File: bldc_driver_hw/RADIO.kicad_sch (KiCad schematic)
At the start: 0 parts

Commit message: wip
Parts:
- added C17: 10uF, Capacitor_SMD:C_0805_2012Metric_Pad1.18x1.45mm_HandSolder, symbol Device:C_Small
- added C18: 100nF, Capacitor_SMD:C_0603_1608Metric_Pad1.08x0.95mm_HandSolder, symbol Device:C_Small
- added D2, D3: LED, LED_SMD:LED_0603_1608Metric, symbol Device:LED
- added R10, R11, R12, R13, R14, R7, R8, R9: 10k, Capacitor_SMD:C_0603_1608Metric, symbol Device:R_Small
- added SW2, SW3: SW_Push, symbol Switch:SW_Push
- added U4: ESP32-C6-MINI-1, RF_Module:ESP32-C6-MINI-1, symbol RF_Module:ESP32-C6-MINI-1
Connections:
- new net: R11.2, SW3.1
- new net: R12.1, SW3.2, U4.23 (IO9)
- new net: D2.2 (A), R13.1
- new net: D3.2 (A), R14.1
- new net: R7.2, SW2.1
- new net: R8.1, SW2.2, U4.8 (EN)
- new net: R10.1, R9.2, U4.22 (IO8)
- new net +3.3V: C17.1, C18.1, R10.2, R12.2, R8.2, U4.3 (3V3)
- new net CONNECTED: R14.2, U4.15 (IO6)
- new net D+: U4.18 (IO13)
- new net D-: U4.17 (IO12)
- new net GND: C17.2, C18.2, D2.1 (K), D3.1 (K), R11.1, R7.1, R9.1, U4.1 (GND), U4.11 (GND), U4.14 (GND), U4.2 (GND), U4.36 (GND), U4.37 (GND), U4.38 (GND), U4.39 (GND), U4.40 (GND), U4.41 (GND), U4.42 (GND), U4.43 (GND), U4.44 (GND), U4.45 (GND), U4.46 (GND), U4.47 (GND), U4.48 (GND), U4.49 (GND), U4.50 (GND), U4.51 (GND), U4.52 (GND), U4.53 (GND)
- new net UART0_RX: U4.30 (RXD0)
- new net UART0_TX: U4.31 (TXD0)
- new net UART_MOTOR_RX: U4.29 (IO23)
- new net UART_MOTOR_TX: U4.28 (IO22)
- new net WIFI_READY: R13.2, U4.16 (IO7)
- no-connect marks 0 -> 12

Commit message: wip
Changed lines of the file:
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@@
 	(wire
 		(pts
-			(xy 93.98 69.85) (xy 82.55 69.85)
+			(xy 93.98 69.85) (xy 76.2 69.85)
 		)
 		(stroke
@@
 	(wire
 		(pts
-			(xy 72.39 67.31) (xy 82.55 67.31)
+			(xy 72.39 67.31) (xy 76.2 67.31)
 		)
 		(stroke
@@
 	(wire
 		(pts
-			(xy 82.55 69.85) (xy 82.55 67.31)
-		)
-		(stroke
+			(xy 76.2 69.85) (xy 76.2 67.31)
+		)
+		(stroke

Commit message: schematic finished pcb in progress
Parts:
- added TP26, TP27, TP28, TP29: TestPoint, TestPoint:TestPoint_Pad_D2.0mm, symbol Connector:TestPoint
- SW2, SW3: footprint (none) -> Button_Switch_SMD:SW_SPST_TL3342
- renumbered C17 to C49, C18 to C50, D2 to D5, D3 to D6, R13 to R25, R14 to R26, R7 to R27, R11 to R28, R10 to R29, R9 to R30, R8 to R31, R12 to R32, U4 to U8
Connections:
- net UART0_RX: now also TP29.1
- net UART0_TX: now also TP28.1
- net UART_MOTOR_RX: now also TP27.1
- net UART_MOTOR_TX: now also TP26.1
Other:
- moved on the sheet: R27, R31, SW2

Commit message: Board finished to review
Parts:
- removed TP26, TP27, TP28, TP29: TestPoint, TestPoint:TestPoint_Pad_D2.0mm, symbol Connector:TestPoint
- added C100, C99: 100nF, Capacitor_SMD:C_0603_1608Metric, symbol Device:C_Small
- C49: footprint Capacitor_SMD:C_0805_2012Metric_Pad1.18x1.45mm_HandSolder -> Capacitor_SMD:C_0603_1608Metric
- C50: footprint Capacitor_SMD:C_0603_1608Metric_Pad1.08x0.95mm_HandSolder -> Capacitor_SMD:C_0603_1608Metric
- R25, R26, R27, R28, R29, R30, R31, R32: footprint Capacitor_SMD:C_0603_1608Metric -> Resistor_SMD:R_0603_1608Metric
- U8: footprint RF_Module:ESP32-C6-MINI-1 -> bldc_driver_footprint:XCVR_ESP32-C6-MINI-1-H4
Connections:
- net CONNECTED: now also U8.9 (IO4); no longer U8.15 (IO6)
- net GND: now also U8.49_1 (GND), U8.49_2 (GND), U8.49_3 (GND), U8.49_4 (GND), U8.49_5 (GND), U8.49_6 (GND), U8.49_7 (GND), U8.49_8 (GND), U8.49_9 (GND), C100.2, C99.2
- net WIFI_READY: now also U8.10 (IO5); no longer U8.16 (IO7)
- net at R32.1, SW3.2, U8.23 (IO9): now also C100.1
- net at R31.1, SW2.2, U8.8 (EN): now also C99.1

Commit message: board finished
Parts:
- added C1: 47uF, Capacitor_Tantalum_SMD:CP_EIA-6032-15_Kemet-U, symbol Device:C_Polarized_Small
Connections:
- net +3.3V: now also C1.1
- net GND: now also C1.2
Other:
- moved on the sheet: C49, C50

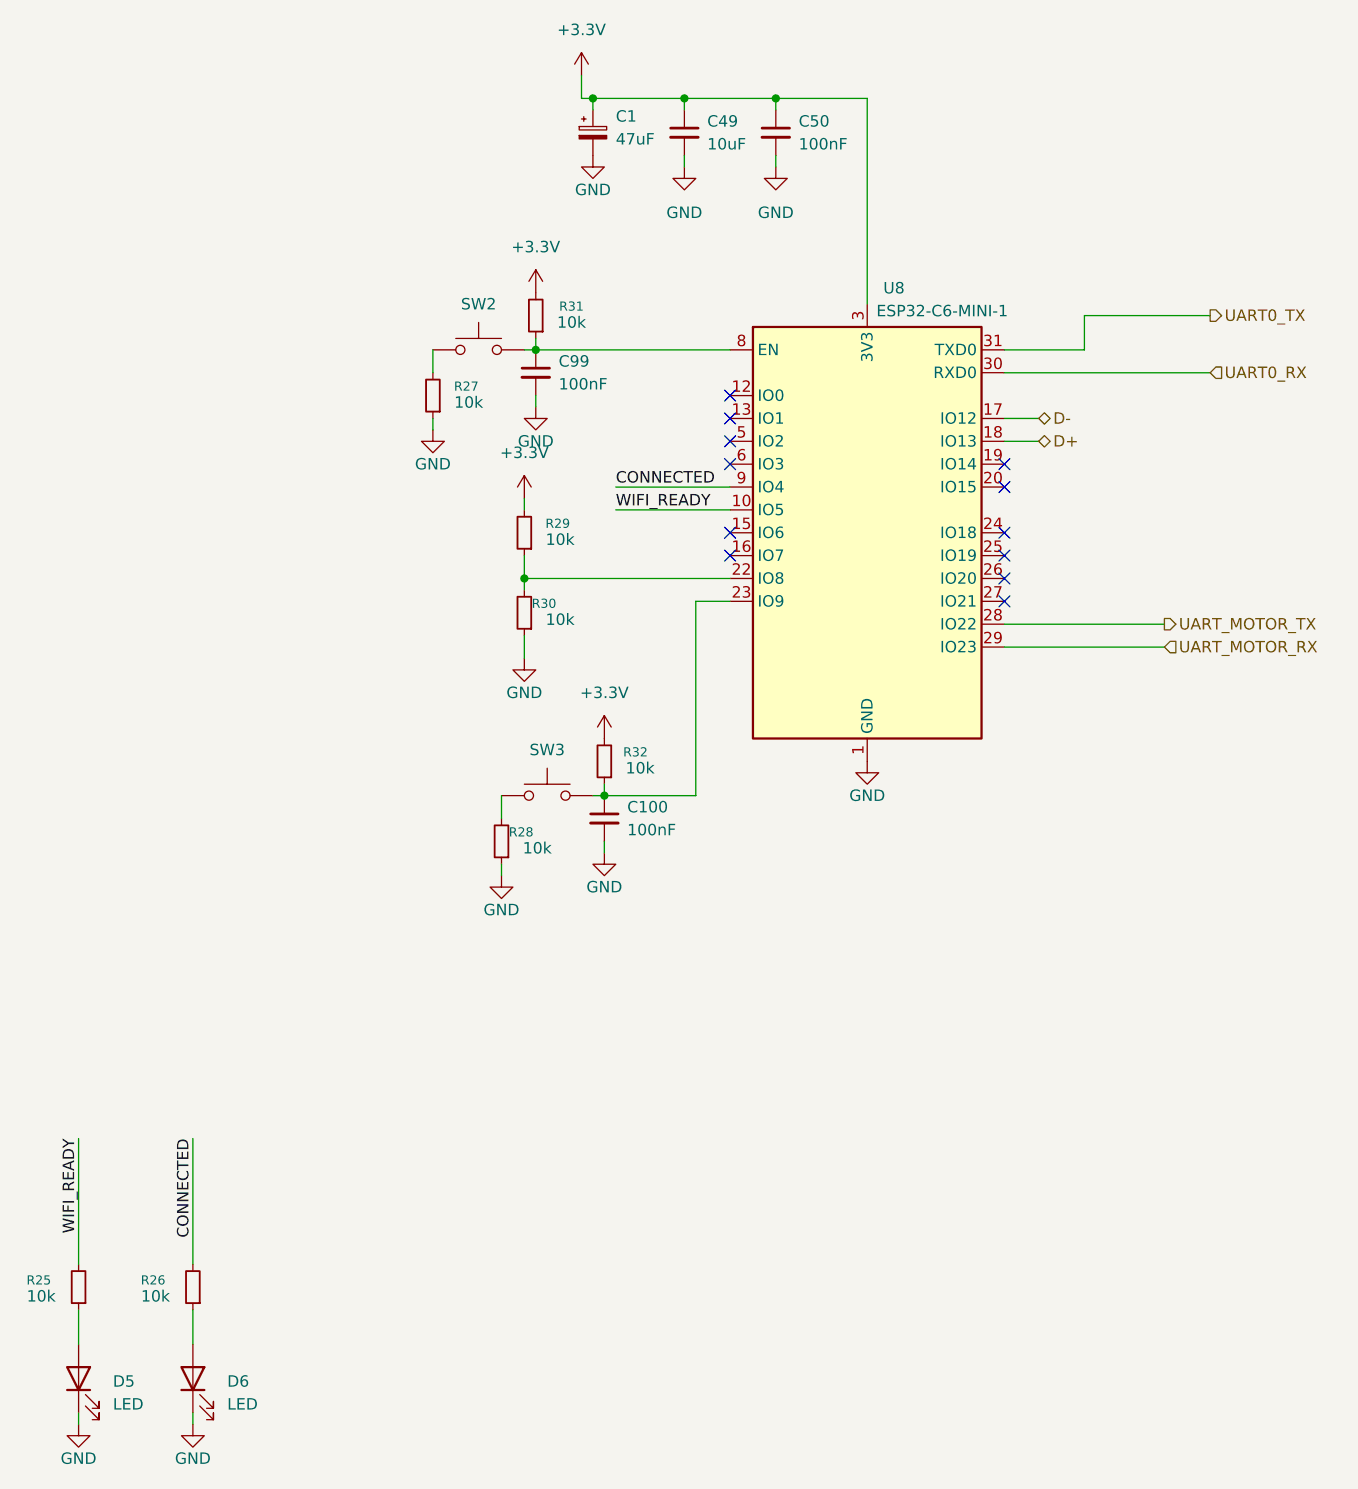
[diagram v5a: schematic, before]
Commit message: added lcsc codes
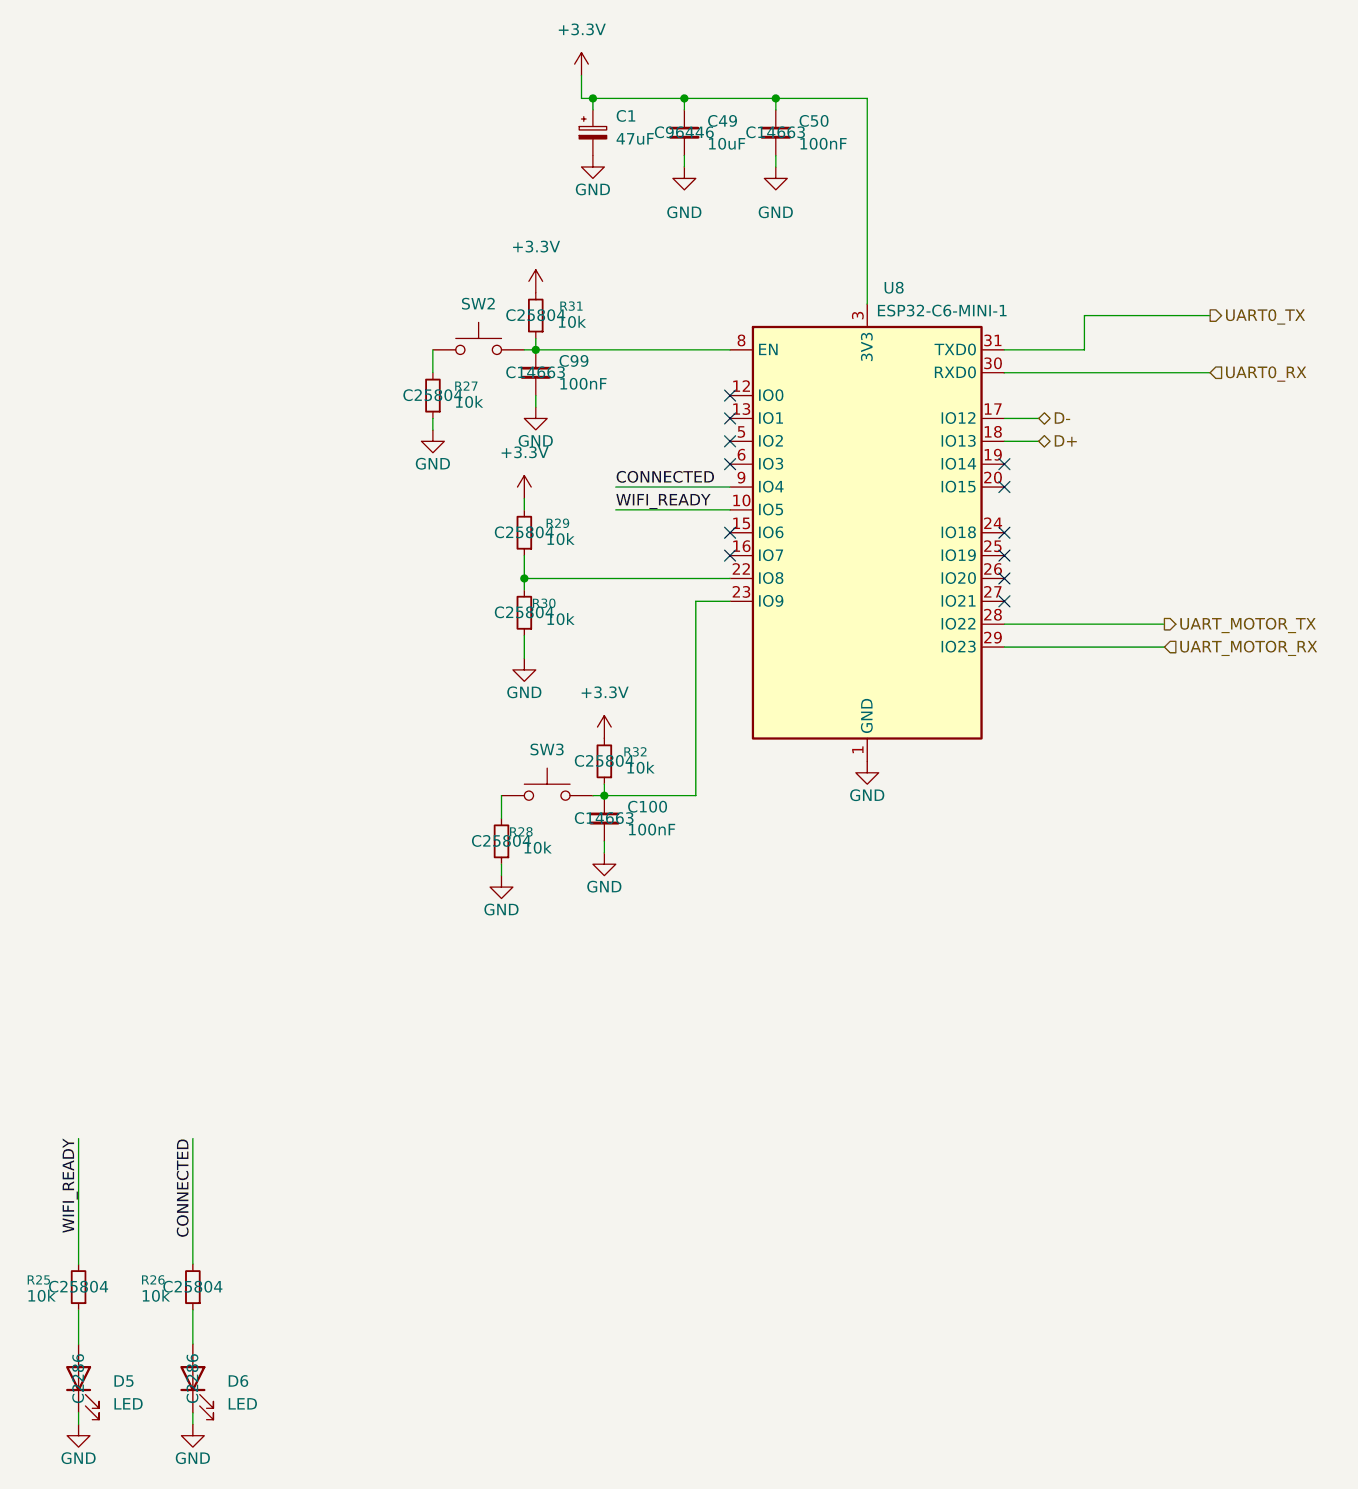
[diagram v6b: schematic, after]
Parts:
- C100, C50, C99: LCSC (none) -> C14663
- C49: LCSC (none) -> C96446
- D5, D6: LCSC (none) -> C2286
- R25, R26, R27, R28, R29, R30, R31, R32: LCSC (none) -> C25804

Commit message: finished_board
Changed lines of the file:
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@@
 		(dnp no)
 		(property "Reference" "R28"
-			(at 72.136 123.444 0)
+			(at 73.406 123.444 0)
 			(effects
 				(font
@@
 					(size 1.27 1.27)
 				)
+				(hide yes)
 			)
 		)
@@
 					(size 1.27 1.27)
 				)
+				(hide yes)
 			)
 		)
@@
 		(on_board yes)
 		(dnp no)
-		(fields_autoplaced yes)
 		(property "Reference" "#PWR0112"
 			(at 71.12 90.17 0)
@@
 		)
 		(property "Value" "+3.3V"
-			(at 71.12 81.28 0)
+			(at 71.374 82.296 0)
 			(effects
 				(font
@@
 					(size 1.27 1.27)
 				)
+				(hide yes)
 			)
 		)
@@
 					(size 1.27 1.27)
 				)
+				(hide yes)
 			)
 		)
@@
 					(size 1.27 1.27)
 				)
+				(hide yes)
 			)
 		)
@@
 					(size 1.27 1.27)
 				)
+				(hide yes)
 			)
 		)
@@
 					(size 1.27 1.27)
 				)
+				(hide yes)
 			)
 		)
@@
 					(size 1.27 1.27)
 				)
+				(hide yes)
 			)
 		)
@@
 					(size 1.27 1.27)
 				)
+				(hide yes)
 			)
 		)
@@
 					(size 1.27 1.27)
 				)
+				(hide yes)
 			)
 		)
@@
 		)
 		(property "LCSC" "C14663"
-			(at 80.01 121.92 0)
-			(effects
-				(font
-					(size 1.27 1.27)
-				)
+			(at 82.55 124.4662 0)
+			(effects
+				(font
+					(size 1.27 1.27)
+				)
+				(justify left)
+				(hide yes)
 			)
 		)
@@
 					(size 1.27 1.27)
 				)
+				(hide yes)
 			)
 		)
@@
 					(size 1.27 1.27)
 				)
+				(hide yes)
 			)
 		)
@@
 					(size 1.27 1.27)
 				)
-			)
-		)
+				(hide yes)
+			)
+		)

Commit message: finished
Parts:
- C1, U8: now left out of the parts list
- SW2, SW3: LCSC (none) -> C318884
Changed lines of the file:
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@@
 		(unit 1)
 		(exclude_from_sim no)
-		(in_bom yes)
+		(in_bom no)
 		(on_board yes)
 		(dnp no)
@@
 			)
 		)
+		(property "LCSC" "C318884"
+			(at 66.04 69.85 0)
+			(effects
+				(font
+					(size 1.27 1.27)
+				)
+			)
+		)
 		(pin "1"
 		)
@@
 			)
 		)
+		(property "LCSC" "C318884"
+			(at 73.66 119.38 0)
+			(effects
+				(font
+					(size 1.27 1.27)
+				)
+			)
+		)
 		(pin "1"
 		)
@@
 		(unit 1)
 		(exclude_from_sim no)
-		(in_bom yes)
-		(on_board yes)
-		(dnp no)
+		(in_bom no)
+		(on_board yes)
+		(dnp no)
